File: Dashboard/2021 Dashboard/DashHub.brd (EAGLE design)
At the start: 86.4 x 66 mm, 25 parts, among them J1 LEFT, J2 RIGHT, U1 ALLEGRO_MICROSYSTEMS_ACS722LL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

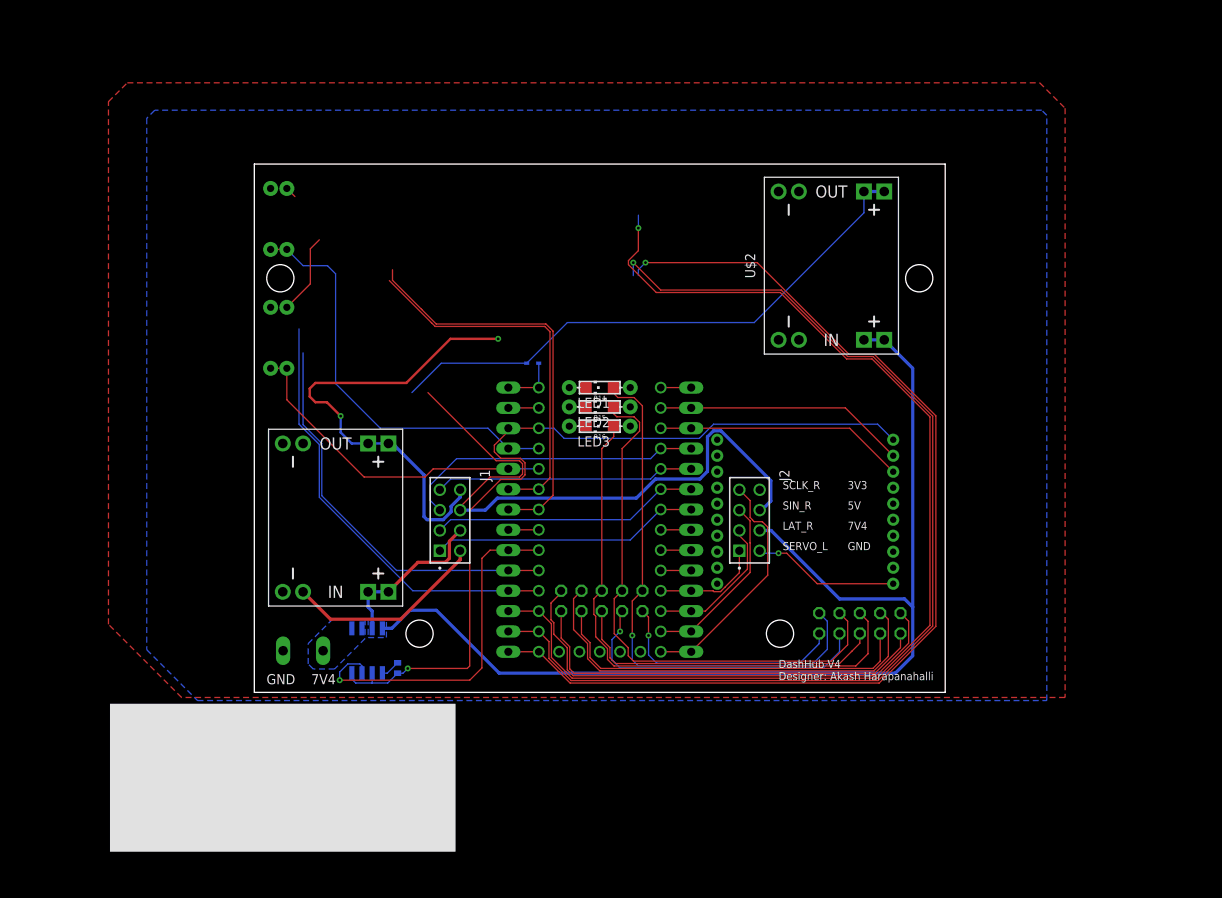
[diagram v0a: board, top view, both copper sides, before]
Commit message: Moved phat connector
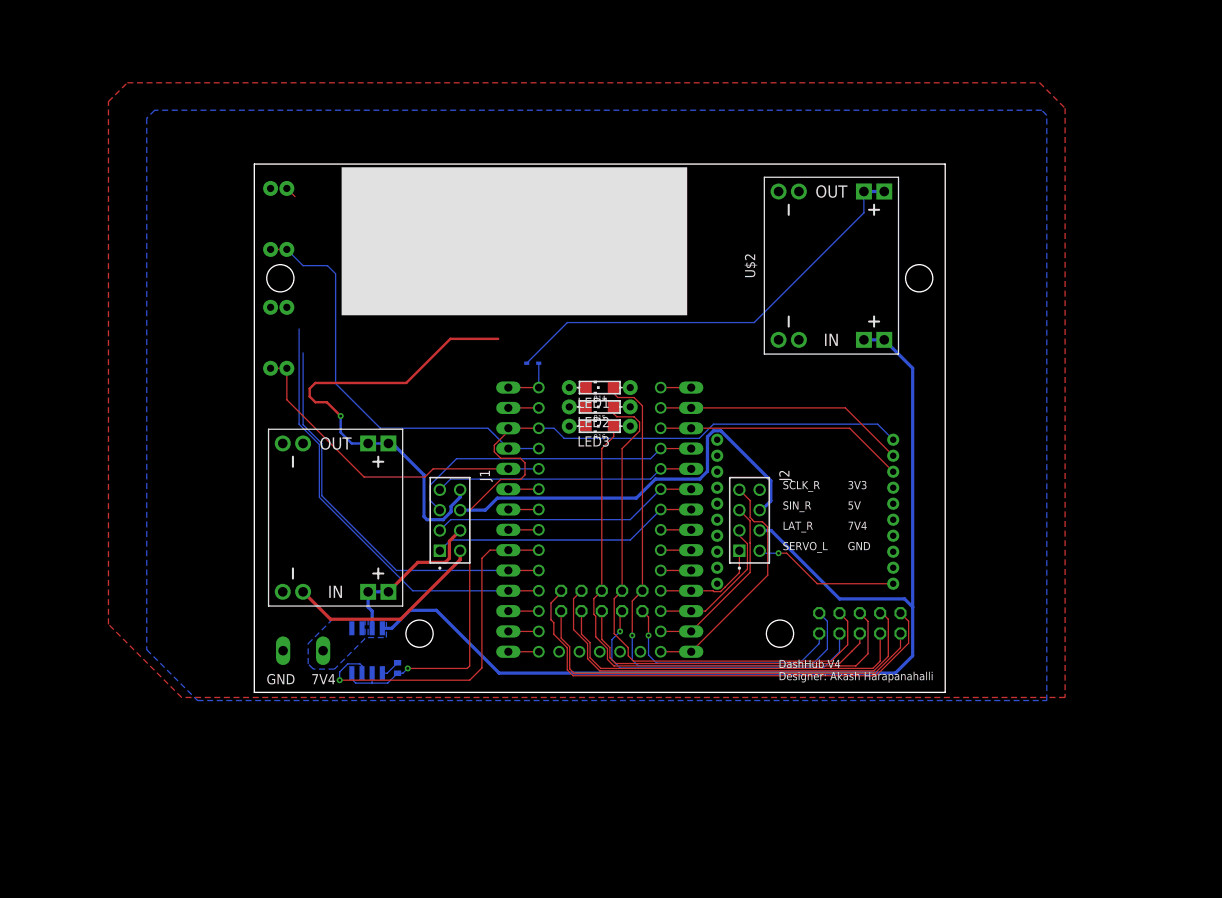
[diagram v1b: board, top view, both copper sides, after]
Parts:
- moved U$4 73.0 mm to (-10.7, 23.4)
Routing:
- net LAT_D: track 139.7 -> 3.81 mm, vias 1 -> 0
- net SIN_D: track 132.9 -> 3.81 mm, vias 1 -> 0
- net SCLK_D: track 130.5 -> 3.81 mm, vias 1 -> 0
- net ANALOG2: track 50.9 -> 3.81 mm
- net ANALOG1: track 46.8 -> 3.81 mm
- net 5V: track 150.2 -> 107.6 mm
- net N$23: track 10.1 -> 0.00 mm
- net 3.3V_BUCK: vias 2 -> 1

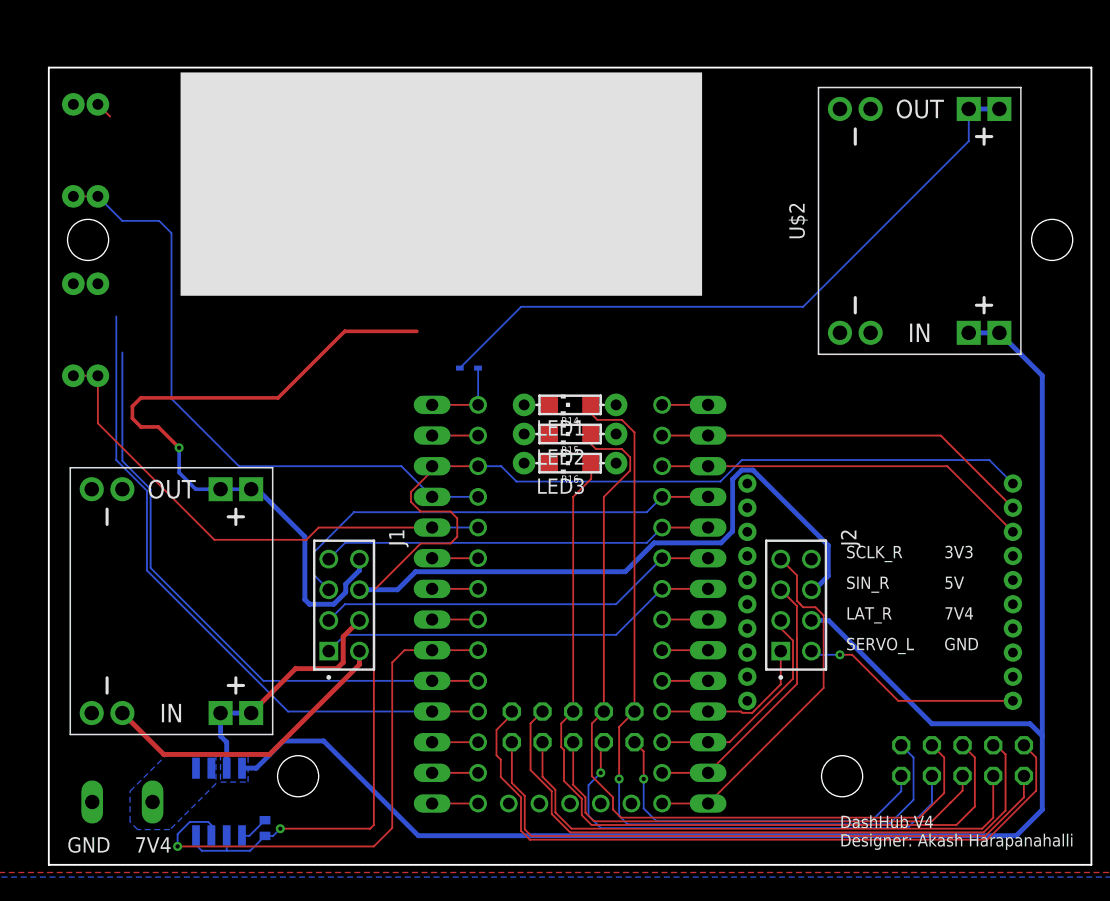
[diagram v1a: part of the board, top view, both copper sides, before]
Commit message: Put new LED driver into dashhub
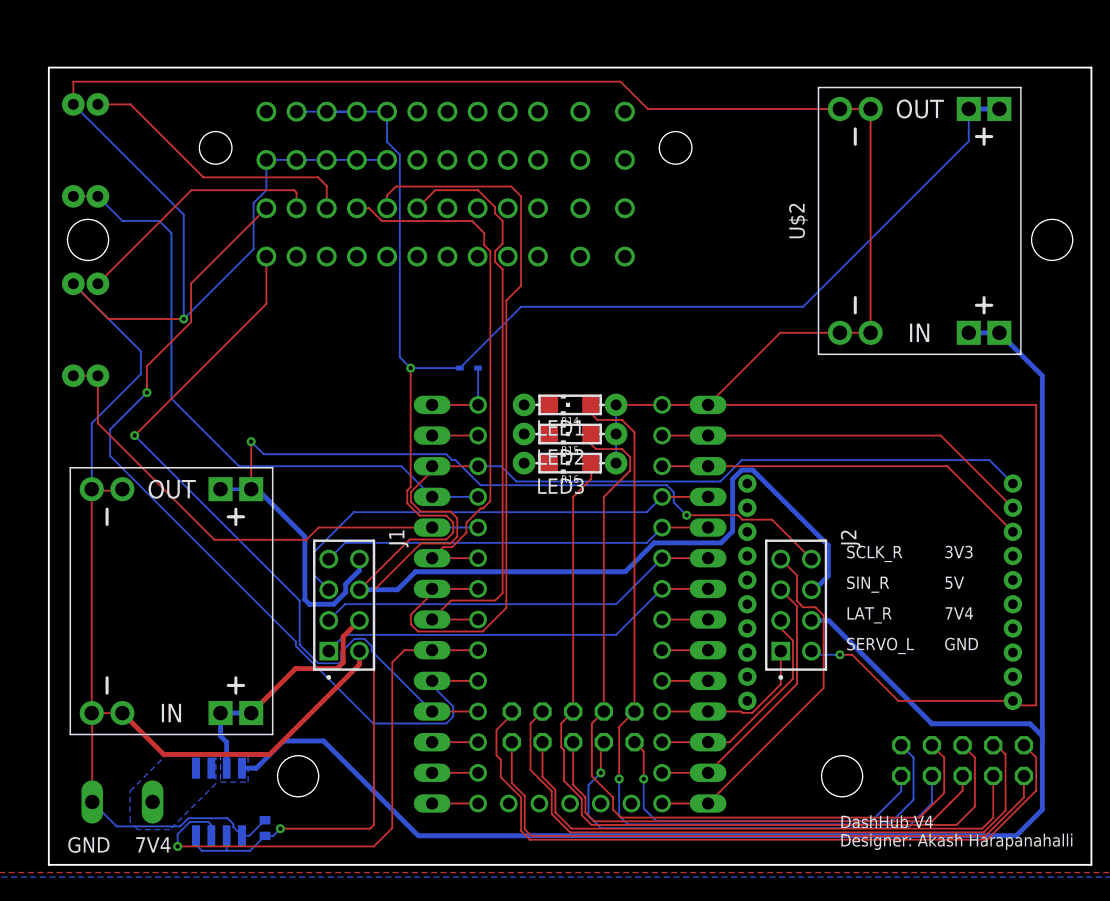
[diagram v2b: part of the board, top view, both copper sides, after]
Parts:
- U$4: device GTOR - Connectors:366380003 -> GTOR - Connectors:48CKTRASCMCHEADER
- moved U$4 0.51 mm to (-10.2, 23.4), flipped to the bottom
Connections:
- removed net N$5: U$4.P$1D
- removed net N$6: U$4.P$1E
- removed net N$7: U$4.P$2D
- removed net N$8: U$4.P$2E
- net 5V: now also U$4.P$1D, U$4.P$1E
- net AUX_RX: now also U$4.P$4A; no longer U$4.P$3A
- net AUX_TX: now also U$4.P$3A; no longer U$4.P$2A
- net GND: now also U$4.P$2A, U$4.P$2D, U$4.P$2E; no longer U$4.P$1A
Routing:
- net GND: track 49.9 -> 340.3 mm, vias 1 -> 2
- net 5V: track 107.6 -> 170.1 mm, vias 0 -> 1
- net ANALOG2: track 3.81 -> 63.8 mm
- net ANALOG3: track 3.81 -> 50.9 mm
- net ANALOG1: track 3.81 -> 44.9 mm
- net N$24: track 1.44 -> 23.6 mm
- net AUX_TX: track 49.8 -> 71.4 mm, vias 0 -> 1
- net N$23: track 0.00 -> 21.0 mm
- net 3.3V_BUCK: track 59.1 -> 75.9 mm, vias 1 -> 2
- net AUX_RX: track 54.4 -> 61.8 mm, vias 0 -> 1

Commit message: Added GPS
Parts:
- added U$5: DIYMALL_6M_GPS_BREAKOUT, GTOR - Breakout Boards:DIYMALL_6M_GPS_BREAKOUT
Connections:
- new net +3V3: U$5.VCC
- new net GPS_RX: U$5.RX
- new net GPS_TX: U$5.TX
- net GND: now also U$5.GND
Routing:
- net GND: track 340.3 -> 336.4 mm
- net 3.3V_TEENSY: track 105.8 -> 108.7 mm
- net 5V: track 170.1 -> 169.1 mm
- net XBEE_RX: track 31.5 -> 32.4 mm
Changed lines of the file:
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@@
 <layer number="19" name="Unrouted" color="6" fill="1" visible="yes" active="yes"/>
 <layer number="20" name="Dimension" color="24" fill="1" visible="yes" active="yes"/>
-<layer number="21" name="tPlace" color="7" fill="1" visible="no" active="yes"/>
-<layer number="22" name="bPlace" color="7" fill="1" visible="no" active="yes"/>
+<layer number="21" name="tPlace" color="7" fill="1" visible="yes" active="yes"/>
+<layer number="22" name="bPlace" color="7" fill="1" visible="yes" active="yes"/>
 <layer number="23" name="tOrigins" color="15" fill="1" visible="yes" active="yes"/>
 <layer number="24" name="bOrigins" color="15" fill="1" visible="yes" active="yes"/>
@@
 <layer number="37" name="tTest" color="7" fill="1" visible="no" active="yes"/>
 <layer number="38" name="bTest" color="7" fill="1" visible="no" active="yes"/>
-<layer number="39" name="tKeepout" color="4" fill="11" visible="yes" active="yes"/>
+<layer number="39" name="tKeepout" color="4" fill="11" visible="no" active="yes"/>
 <layer number="40" name="bKeepout" color="1" fill="11" visible="yes" active="yes"/>
-<layer number="41" name="tRestrict" color="4" fill="10" visible="yes" active="yes"/>
+<layer number="41" name="tRestrict" color="4" fill="10" visible="no" active="yes"/>
 <layer number="42" name="bRestrict" color="1" fill="10" visible="yes" active="yes"/>
 <layer number="43" name="vRestrict" color="2" fill="10" visible="no" active="yes"/>
@@
 <layer number="49" name="Reference" color="7" fill="1" visible="no" active="yes"/>
 <layer number="50" name="dxf" color="7" fill="1" visible="no" active="no"/>
-<layer number="51" name="tDocu" color="7" fill="1" visible="yes" active="yes"/>
+<layer number="51" name="tDocu" color="7" fill="1" visible="no" active="yes"/>
 <layer number="52" name="bDocu" color="7" fill="1" visible="yes" active="yes"/>
 <layer number="53" name="tGND_GNDA" color="7" fill="1" visible="no" active="no"/>
@@
 </element>
 <element name="U$4" library="GTOR - Connectors" package="48CKTRASCMCHEADER" value="48CKTRASCMCHEADER" x="-10.16" y="23.368" smashed="yes" rot="MR0"/>
+<element name="U$5" library="GTOR - Breakout Boards" package="DIYMALL_6M_GPS_BREAKOUT" value="DIYMALL_6M_GPS_BREAKOUT" x="75.692" y="24.384" smashed="yes" rot="R179.9"/>
 </elements>
 <signals>
@@
 <wire x1="11.43" y1="5.08" x2="17.399" y2="11.049" width="0.1524" layer="1"/>
 <wire x1="17.399" y1="11.049" x2="22.352" y2="11.049" width="0.1524" layer="1"/>
-<wire x1="11.43" y1="5.08" x2="38.608" y2="5.08" width="0.1524" layer="1"/>
-<wire x1="38.608" y1="5.08" x2="38.608" y2="-19.812" width="0.1524" layer="1"/>
+<wire x1="38.608" y1="-1.524" x2="38.608" y2="-19.812" width="0.1524" layer="1"/>
 <wire x1="38.608" y1="-19.812" x2="37.0538" y2="-19.812" width="0.1524" layer="1"/>
 <wire x1="37.0538" y1="-19.812" x2="36.6794" y2="-19.4376" width="0.1524" layer="1"/>
@@
 <wire x1="-20.16" y1="25.368" x2="-17.66" y2="25.368" width="0.1524" layer="16"/>
 <wire x1="-17.66" y1="25.368" x2="-15.16" y2="25.368" width="0.1524" layer="16"/>
+<contactref element="U$5" pad="GND"/>
+<wire x1="37.084" y1="0" x2="38.608" y2="-1.524" width="0.1524" layer="1"/>
+<wire x1="37.084" y1="0" x2="16.51" y2="0" width="0.1524" layer="1"/>
+<wire x1="11.43" y1="5.08" x2="16.51" y2="0" width="0.1524" layer="1"/>
+<wire x1="36.6794" y1="-19.4376" x2="74.16810625" y2="10.6966375" width="0" layer="19" extent="1-1"/>
 </signal>
 <signal name="LAT_L">
@@
 <wire x1="-11.43" y1="0" x2="-7.62" y2="0" width="0.1524" layer="1"/>
 <wire x1="-7.62" y1="0" x2="-5.715" y2="0" width="0.1524" layer="16"/>
-<wire x1="34.7338" y1="0.508" x2="36.6794" y2="-1.4376" width="0.1524" layer="16"/>
+<wire x1="33.1234" y1="-4.9936" x2="36.6794" y2="-1.4376" width="0.1524" layer="16"/>
+<wire x1="33.1234" y1="-4.9936" x2="20.9314" y2="-4.9936" width="0.1524" layer="16"/>
+<wire x1="20.9314" y1="-4.9936" x2="15.4298" y2="0.508" width="0.1524" layer="16"/>
 <wire x1="-5.715" y1="0" x2="-4.445" y2="-1.27" width="0.1524" layer="16"/>
 <wire x1="-4.445" y1="-1.27" x2="12.446" y2="-1.27" width="0.1524" layer="16"/>
 <wire x1="12.446" y1="-1.27" x2="14.224" y2="0.508" width="0.1524" layer="16"/>
-<wire x1="14.224" y1="0.508" x2="34.7338" y2="0.508" width="0.1524" layer="16"/>
+<wire x1="14.224" y1="0.508" x2="15.4298" y2="0.508" width="0.1524" layer="16"/>
 <wire x1="-25.273" y1="-30.622" x2="-26.5026" y2="-31.8516" width="0.1524" layer="16"/>
 <wire x1="-30.5054" y1="-31.8516" x2="-30.988" y2="-31.369" width="0.1524" layer="16"/>
@@
 <wire x1="11.43" y1="2.54" x2="7.62" y2="2.54" width="0.1524" layer="1"/>
 <contactref element="JP1" pad="2"/>
-<wire x1="11.43" y1="2.54" x2="30.7018" y2="2.54" width="0.1524" layer="1"/>
-<wire x1="30.7018" y1="2.54" x2="36.6794" y2="-3.4376" width="0.1524" layer="1"/>
+<wire x1="11.43" y1="2.54" x2="13.4298" y2="2.54" width="0.1524" layer="1"/>
+<wire x1="20.4234" y1="-4.4536" x2="13.4298" y2="2.54" width="0.1524" layer="1"/>
+<wire x1="35.6634" y1="-4.4536" x2="36.6794" y2="-3.4376" width="0.1524" layer="1"/>
+<wire x1="35.6634" y1="-4.4536" x2="20.4234" y2="-4.4536" width="0.1524" layer="1"/>
 </signal>
 <signal name="XBEE_TX">
@@
 <wire x1="11.43" y1="0" x2="7.62" y2="0" width="0.1524" layer="1"/>
 <contactref element="JP1" pad="3"/>
-<wire x1="11.43" y1="0" x2="31.2418" y2="0" width="0.1524" layer="1"/>
-<wire x1="31.2418" y1="0" x2="36.6794" y2="-5.4376" width="0.1524" layer="1"/>
+<wire x1="11.43" y1="0" x2="14.9858" y2="0" width="0.1524" layer="1"/>
+<wire x1="20.4234" y1="-5.4376" x2="36.6794" y2="-5.4376" width="0.1524" layer="1"/>
+<wire x1="20.4234" y1="-5.4376" x2="14.9858" y2="0" width="0.1524" layer="1"/>
 </signal>
 <signal name="N$2">
@@
 <contactref element="U$2" pad="OUT+.1"/>
 <contactref element="U$2" pad="OUT+.2"/>
-<wire x1="-9.132" y1="8.128" x2="-4.052" y2="13.208" width="0.1524" layer="16"/>
-<wire x1="-4.052" y1="13.208" x2="19.304" y2="13.208" width="0.1524" layer="16"/>
-<wire x1="33.02" y1="26.924" x2="33.02" y2="29.591" width="0.1524" layer="16"/>
-<wire x1="19.304" y1="13.208" x2="33.02" y2="26.924" width="0.1524" layer="16"/>
+<wire x1="-9.132" y1="8.128" x2="-9.132" y2="9.144" width="0.1524" layer="16"/>
+<wire x1="1.536" y1="19.812" x2="-9.132" y2="9.144" width="0.1524" layer="16"/>
+<wire x1="33.02" y1="29.591" x2="27.432" y2="29.591" width="0.1524" layer="16"/>
 <wire x1="33.02" y1="29.591" x2="35.56" y2="29.591" width="0.4064" layer="16"/>
 <contactref element="U$4" pad="P$1B"/>
@@
 <wire x1="-13.208" y1="8.128" x2="-14.1064" y2="9.0264" width="0.1524" layer="16"/>
 <wire x1="-14.1064" y1="9.0264" x2="-14.1064" y2="25.80441875" width="0.1524" layer="16"/>
-<wire x1="-22.66" y1="29.368" x2="-20.32" y2="29.368" width="0.1524" layer="16"/>
-<wire x1="-20.32" y1="29.368" x2="-20.16" y2="29.368" width="0.1524" layer="16"/>
+<wire x1="-22.66" y1="29.368" x2="-20.16" y2="29.368" width="0.1524" layer="16"/>
 <wire x1="-20.16" y1="29.368" x2="-15.16" y2="29.368" width="0.1524" layer="16"/>
 <wire x1="-17.66" y1="29.368" x2="-20.16" y2="29.368" width="0.1524" layer="16"/>
+<wire x1="25.7748" y1="27.9338" x2="14.2302" y2="27.9338" width="0.1524" layer="16"/>
+<wire x1="14.2302" y1="27.9338" x2="6.1084" y2="19.812" width="0.1524" layer="16"/>
+<wire x1="27.432" y1="29.591" x2="25.7748" y2="27.9338" width="0.1524" layer="16"/>
+<wire x1="6.1084" y1="19.812" x2="1.536" y2="19.812" width="0.1524" layer="16"/>
 </signal>
 <signal name="3.3V_BUCK">
@@
 <wire x1="-5.588" y1="20.30598125" x2="-5.588" y2="18.43001875" width="0.1524" layer="1"/>
 </signal>
+<signal name="GPS_TX">
+<contactref element="U$5" pad="TX"/>
+</signal>
+<signal name="GPS_RX">
+<contactref element="U$5" pad="RX"/>
+</signal>
+<signal name="+3V3">
+<contactref element="U$5" pad="VCC"/>
+</signal>
 </signals>
